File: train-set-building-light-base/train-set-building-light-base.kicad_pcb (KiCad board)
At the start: 2 copper layers, 139.7 x 25.4 mm, 8 parts, among them J1 Screw_Terminal_01x02

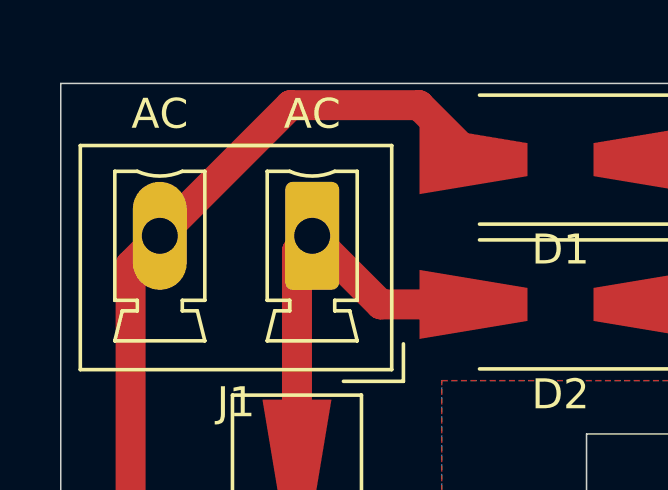
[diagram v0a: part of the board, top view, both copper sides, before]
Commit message: Updating to KiCad 9.0
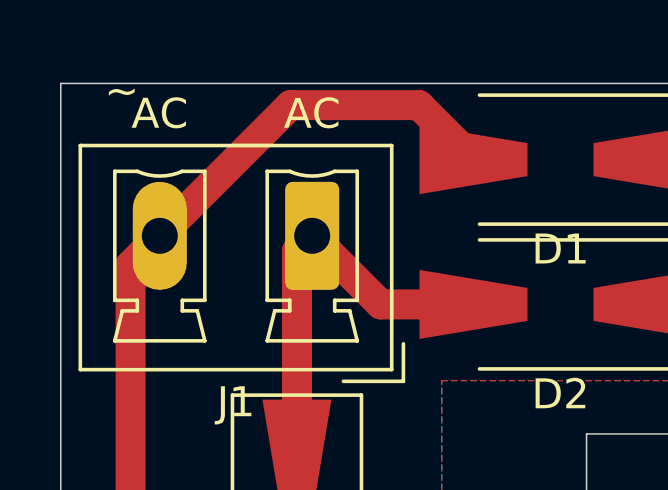
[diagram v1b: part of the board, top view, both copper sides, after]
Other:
- net class Default removed
